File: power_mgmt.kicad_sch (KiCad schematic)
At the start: 54 parts

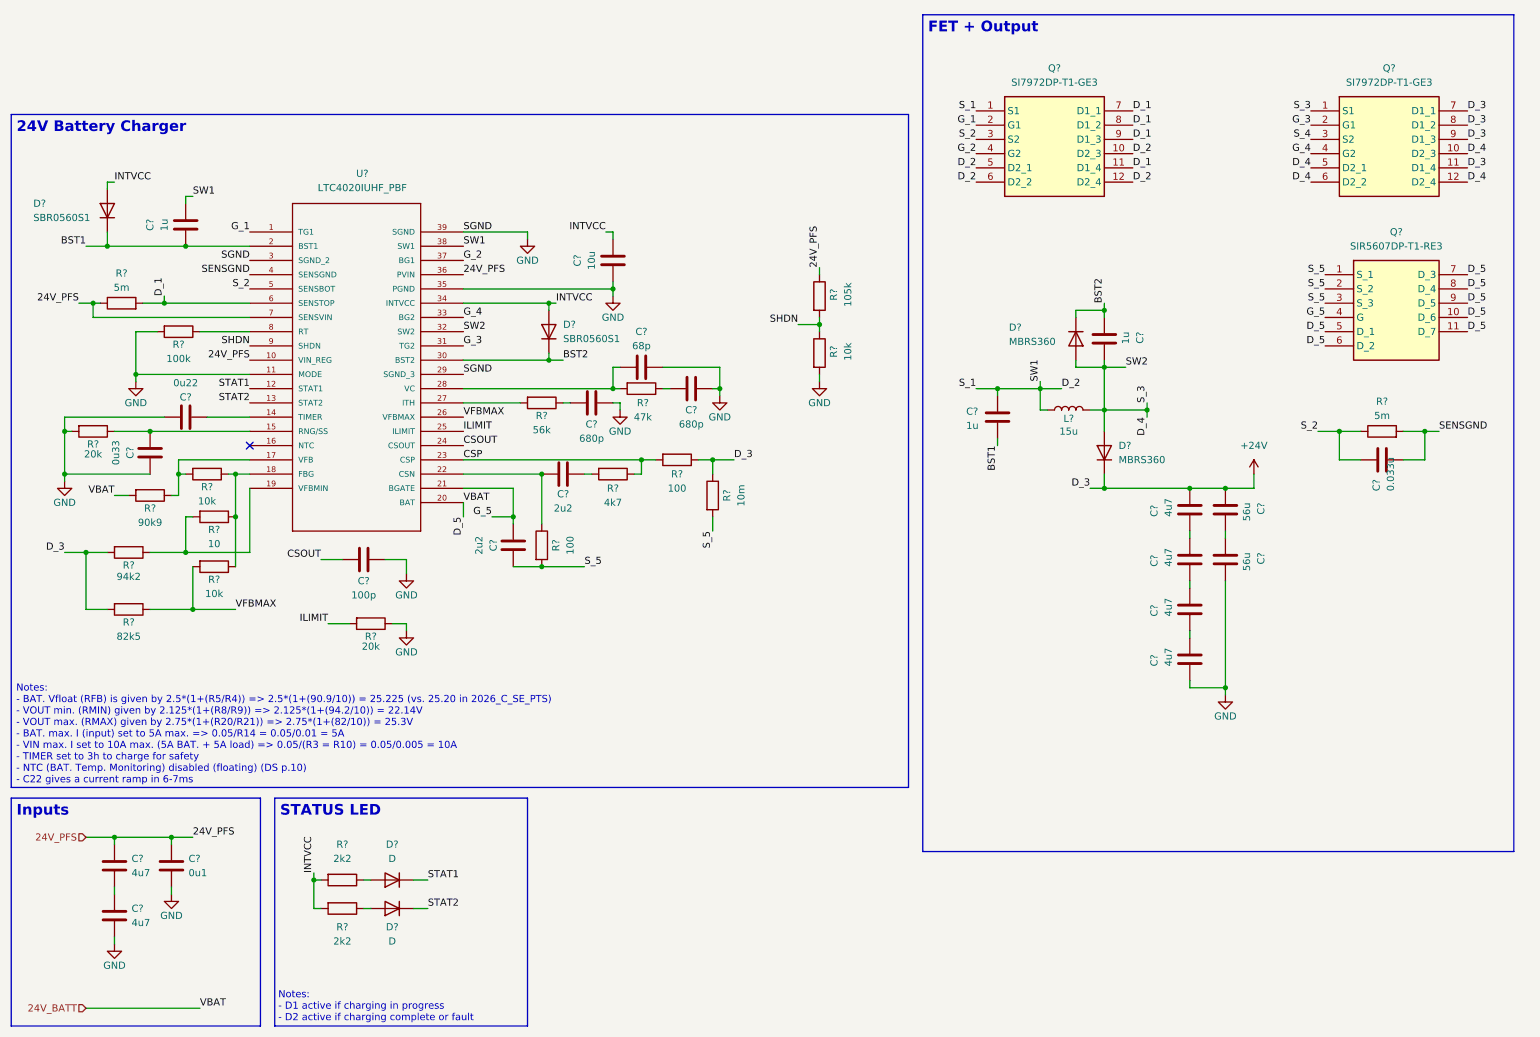
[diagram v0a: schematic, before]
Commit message: add: power MUX + global labels
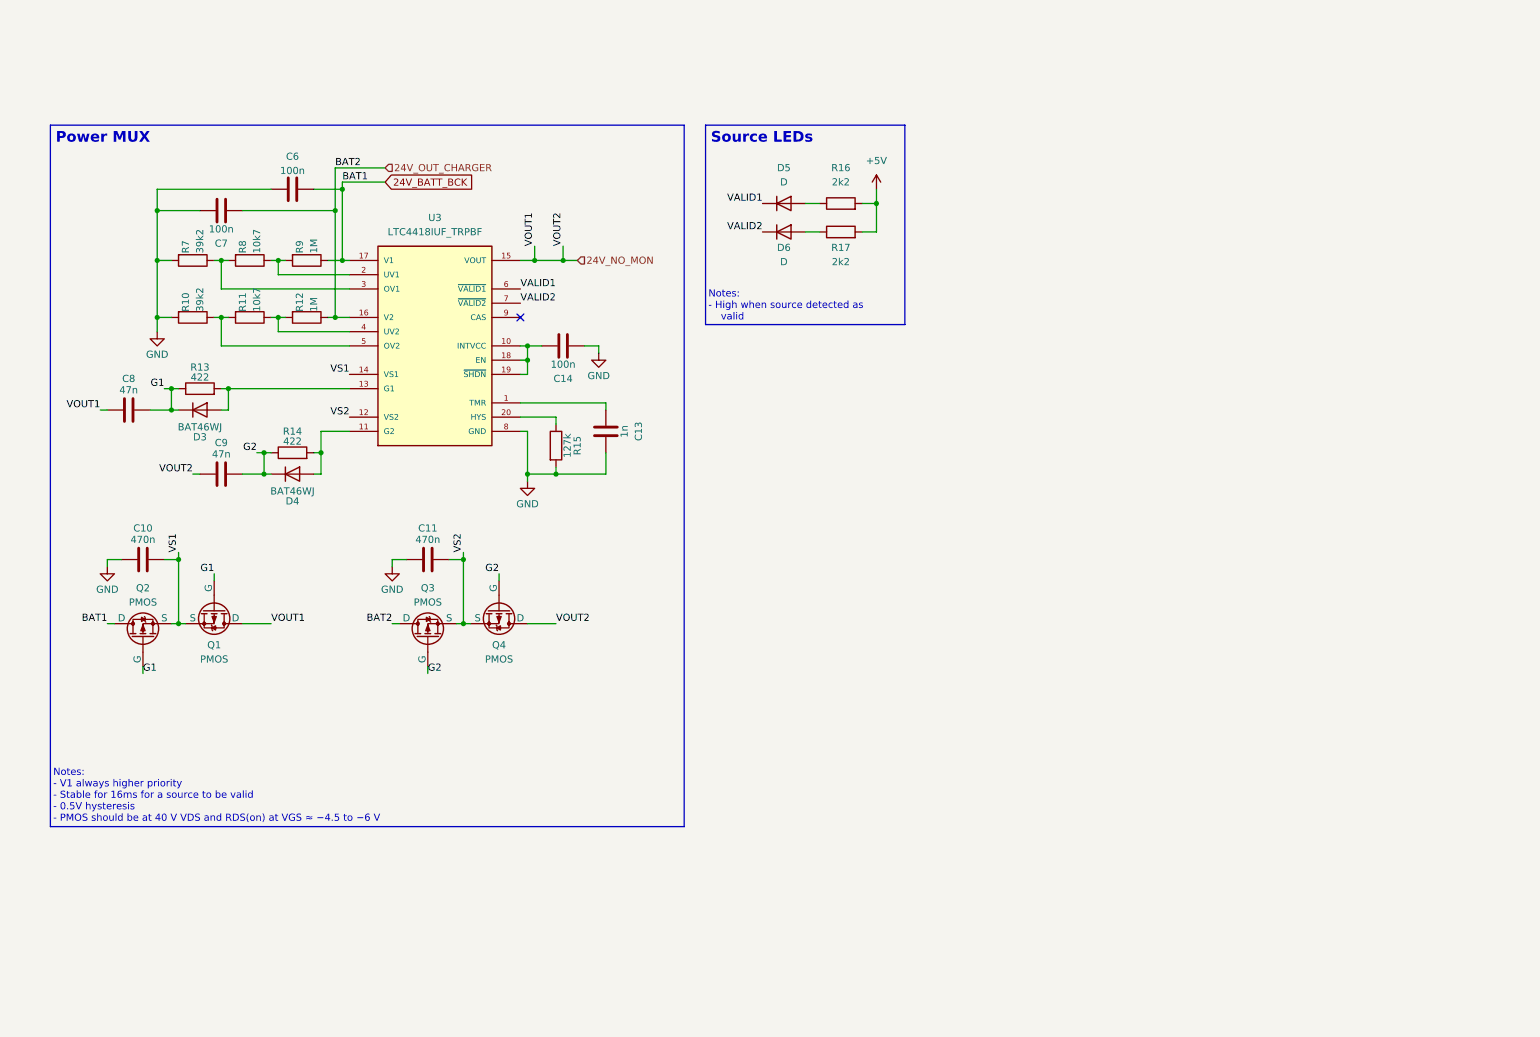
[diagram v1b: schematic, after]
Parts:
- removed C? (x6): 4u7, symbol Device:C
- removed C?: 0u22, symbol Device:C
- removed C? (x2): 680p, symbol Device:C
- removed C?: 68p, symbol Device:C
- removed C? (x3): 1u, symbol Device:C
- removed C?: 10u, symbol Device:C
- removed C? (x2): 56u, symbol Device:C
- removed C?: 0.033u, symbol Device:C
- removed C?: 0u1, symbol Device:C
- removed C? (x2): 2u2, symbol Device:C
- removed C?: 0u33, symbol Device:C
- removed C?: 100p, symbol Device:C
- removed D? (x2): D, symbol Device:D
- removed D? (x2): MBRS360, symbol Device:D
- removed D? (x2): SBR0560S1, symbol Device:D
- removed L?: 15u, symbol Device:L
- removed Q?: SIR5607DP-T1-RE3, SI7852ADPT1GE3, symbol SIR5607DP-T1-RE3:SIR5607DP-T1-RE3
- removed Q? (x2): SI7972DP-T1-GE3, SI7288DPT1GE3, symbol SI7972DP-T1-GE3:SI7972DP-T1-GE3
- removed R? (x2): 100, symbol Device:R
- removed R?: 10m, symbol Device:R
- removed R?: 82k5, symbol Device:R
- removed R? (x2): 5m, symbol Device:R
- removed R?: 100k, symbol Device:R
- removed R?: 94k2, symbol Device:R
- removed R? (x2): 2k2, symbol Device:R
- removed R?: 10, symbol Device:R
- removed R?: 47k, symbol Device:R
- removed R?: 90k9, symbol Device:R
- removed R? (x2): 20k, symbol Device:R
- removed R?: 105k, symbol Device:R
- removed R? (x3): 10k, symbol Device:R
- removed R?: 56k, symbol Device:R
- removed R?: 4k7, symbol Device:R
- removed U?: LTC4020IUHF_PBF, LTC4020IUHF_PBF:QFN-38_UHF, symbol LTC4020IUHF_PBF:LTC4020IUHF_PBF
- added C10, C11: 470n, symbol Device:C
- added C13: 1n, symbol Device:C
- added C14, C6, C7: 100n, symbol Device:C
- added C8, C9: 47n, symbol Device:C
- added D3, D4: BAT46WJ, symbol Device:D
- added D5, D6: D, symbol Device:D
- added Q1, Q2, Q3, Q4: PMOS, symbol Simulation_SPICE:PMOS
- added R10, R7: 39k2, symbol Device:R
- added R11, R8: 10k7, symbol Device:R
- added R12, R9: 1M, symbol Device:R
- added R13, R14: 422, symbol Device:R
- added R15: 127k, symbol Device:R
- added R16, R17: 2k2, symbol Device:R
- added U3: LTC4418IUF_TRPBF, LTC4418IUF_TRPBF:QFN50P400X400X80-21N, symbol LTC4418IUF_TRPBF:LTC4418IUF_TRPBF
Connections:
- net GND: now also C10.1, C11.1, C13.2, C14.1, C6.1, C7.2, R10.2, R15.2, R7.2, U3.21 (GND), U3.8 (GND)
- new net: R10.1, R11.2, U3.5 (OV2)
- new net: D6.2 (A), R17.1
- new net: D4.2 (A), R14.2, U3.11 (G2)
- new net: D5.2 (A), R16.1
- new net: C13.1, U3.1 (TMR)
- new net: C14.2, U3.10 (INTVCC), U3.18 (EN), U3.19 (~{SHDN})
- new net: D3.2 (A), R13.2, U3.13 (G1)
- new net: R8.1, R9.2, U3.2 (UV1)
- new net: R15.1, U3.20 (HYS)
- new net: R7.1, R8.2, U3.3 (OV1)
- new net: R11.1, R12.2, U3.4 (UV2)
- new net +5V: R16.2, R17.2
- new net 24V_BATT_BCK: C6.2, Q2.1 (D), R9.1, U3.17 (V1)
- new net 24V_NO_MON: C8.1, C9.1, Q1.1 (D), Q4.1 (D), U3.15 (VOUT)
- new net 24V_OUT_CHARGER: C7.1, Q3.1 (D), R12.1, U3.16 (V2)
- new net G1: C8.2, D3.1 (K), Q1.2 (G), Q2.2 (G), R13.1
- new net G2: C9.2, D4.1 (K), Q3.2 (G), Q4.2 (G), R14.1
- new net VALID1: D5.1 (K), U3.6 (~{VALID1})
- new net VALID2: D6.1 (K), U3.7 (~{VALID2})
- new net VS1: C10.2, Q1.3 (S), Q2.3 (S), U3.14 (VS1)
- new net VS2: C11.2, Q3.3 (S), Q4.3 (S), U3.12 (VS2)
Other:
- note added: "Notes: - High when source detected as valid"
- note added: "Notes: - V1 always higher priority - Stable for 16ms for a source to be valid - 0.5V hysteresis - PMOS should be at 40 V VDS and RDS(on) at VGS ≈ −4.5 to −6 V"
- note removed: "Notes: - BAT. Vfloat (RFB) is given by 2.5*(1+(R5/R4)) => 2.5*(1+(90.9/10)) = 25.225 (vs. 25.20 in 2026_C_SE_PTS) - VOUT min. (RMIN) given by 2.125*(1+(R8/R9)) => 2.125*(1+(94.2/10)) = 22.14V - VOUT max. (RMAX) given by 2.75*(1+(R20/R21)) => 2.75*(1+(82/10)) = 25.3V - BAT. max. I (input) set to 5A max. => 0.05/R14 = 0.05/0.01 = 5A - VIN max. I set to 10A max. (5A BAT. + 5A load) => 0.05/(R3 = R10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"
- note removed: "Notes: - D1 active if charging in progress - D2 active if charging complete or fault"
- title: FH2 - Spine -> (none)

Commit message: add: regulator + monitoring
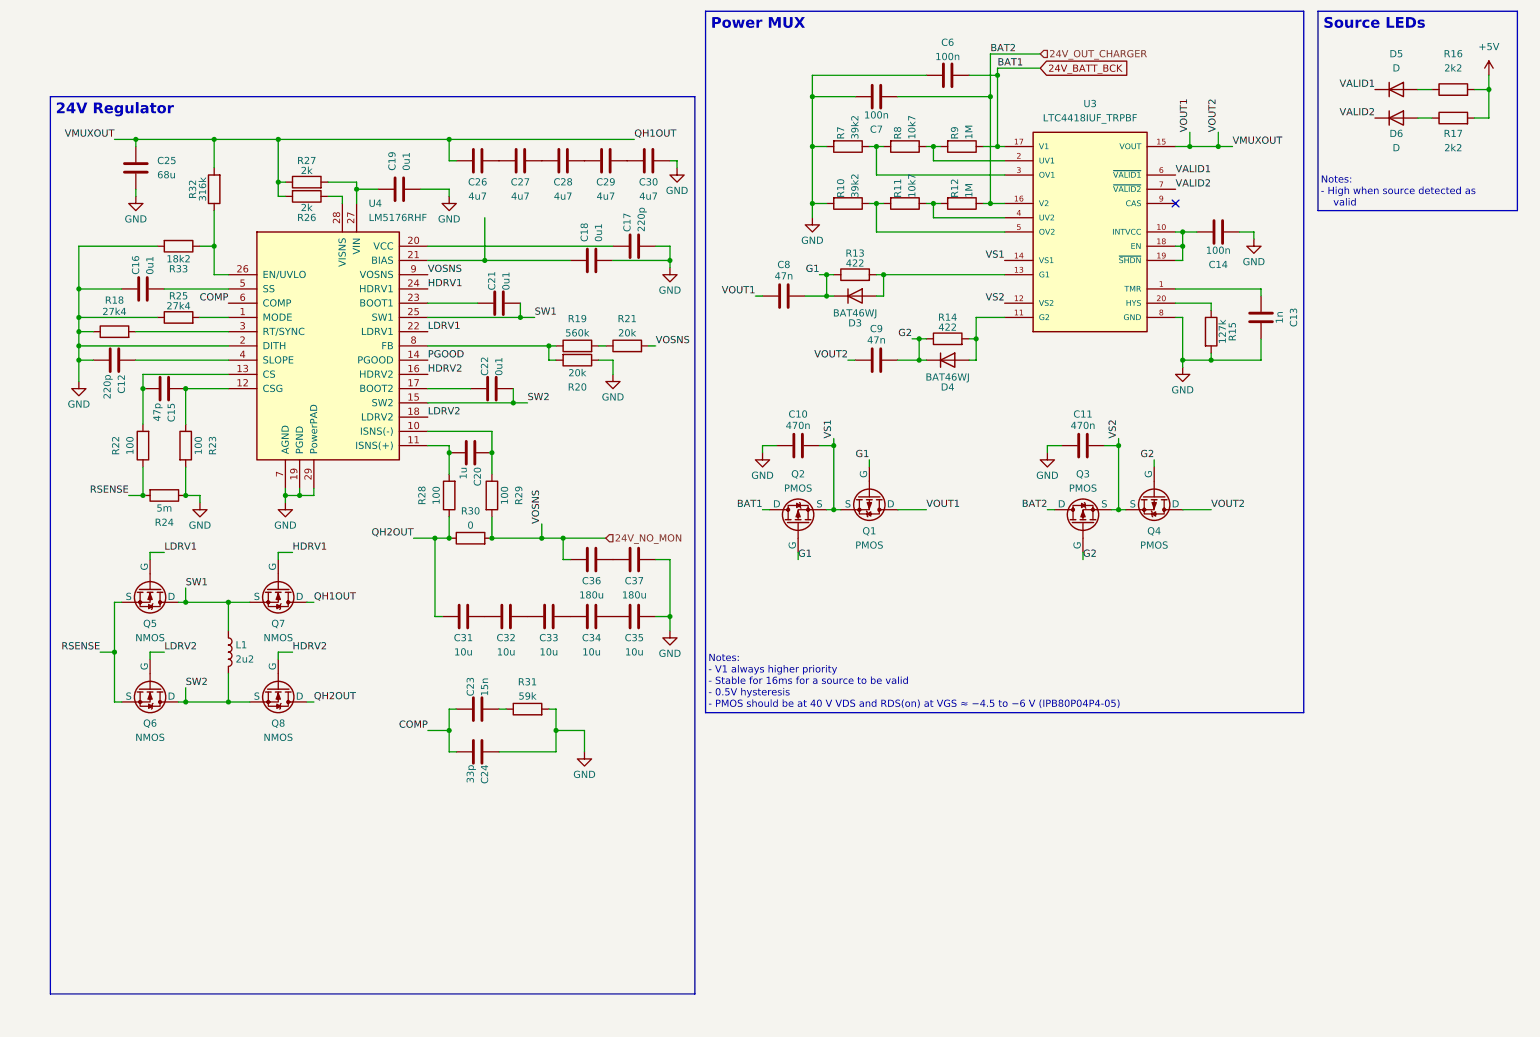
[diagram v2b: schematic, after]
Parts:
- added C12, C17: 220p, symbol Device:C
- added C15: 47p, symbol Device:C
- added C16, C18, C19, C21, C22: 0u1, symbol Device:C
- added C20: 1u, symbol Device:C
- added C23: 15n, symbol Device:C
- added C24: 33p, symbol Device:C
- added C25: 68u, symbol Device:C
- added C26, C27, C28, C29, C30: 4u7, symbol Device:C
- added C31, C32, C33, C34, C35: 10u, symbol Device:C
- added C36, C37: 180u, symbol Device:C
- added L1: 2u2, symbol Device:L
- added Q5, Q6, Q7, Q8: NMOS, symbol Simulation_SPICE:NMOS
- added R18, R25: 27k4, symbol Device:R
- added R19: 560k, symbol Device:R
- added R20, R21: 20k, symbol Device:R
- added R22, R23, R28, R29: 100, symbol Device:R
- added R24: 5m, symbol Device:R
- added R26, R27: 2k, symbol Device:R
- added R30: 0, symbol Device:R
- added R31: 59k, symbol Device:R
- added R32: 316k, symbol Device:R
- added R33: 18k2, symbol Device:R
- added U4: LM5176RHF, Package_DFN_QFN:VQFN-28-1EP_4x5mm_P0.5mm_EP2.55x3.55mm, symbol Regulator_Switching:LM5176RHF
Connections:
- net 24V_NO_MON: now also C36.2, R21.2, R29.2, R30.2, U4.9 (VOSNS); no longer C8.1, C9.1, Q1.1 (D), Q4.1 (D), U3.15 (VOUT)
- net GND: now also C12.2, C16.1, C17.2, C18.2, C19.2, C24.1, C25.2, C30.1, C35.1, C37.1, R18.1, R20.1, R23.2, R24.1, R25.1, R31.2, R33.2, U4.19 (PGND), U4.2 (DITH), U4.29 (PowerPAD), U4.7 (AGND)
- new net: R19.1, R20.2, U4.8 (FB)
- new net: R19.2, R21.1
- new net: R25.2, U4.1 (MODE)
- new net: C20.1, R29.1, U4.10 (ISNS(-))
- new net: C20.2, R28.2, U4.11 (ISNS(+))
- new net: C15.1, R23.1, U4.12 (CSG)
- new net: C15.2, R22.2, U4.13 (CS)
- new net: C22.1, U4.17 (BOOT2)
- new net: C17.1, U4.20 (VCC)
- new net: C18.1, U4.21 (BIAS)
- new net: C21.1, U4.23 (BOOT1)
- new net: R32.1, R33.1, U4.26 (EN/UVLO)
- new net: C19.1, R27.2, U4.27 (VIN)
- new net: R26.1, U4.28 (VISNS)
- new net: R18.2, U4.3 (RT/SYNC)
- new net: C12.1, U4.4 (SLOPE)
- new net: C16.2, U4.5 (SS)
- new net: C23.2, R31.1
- new net: C36.1, C37.2
- new net: C34.1, C35.2
- new net: C33.1, C34.2
- new net: C29.1, C30.2
- new net: C31.1, C32.2
- new net: C26.1, C27.2
- new net: C27.1, C28.2
- new net: C28.1, C29.2
- new net: C32.1, C33.2
- new net COMP: C23.1, C24.2, U4.6 (COMP)
- new net HDRV1: Q7.2 (G), U4.24 (HDRV1)
- new net HDRV2: Q8.2 (G), U4.16 (HDRV2)
- new net LDRV1: Q5.2 (G), U4.22 (LDRV1)
- new net LDRV2: Q6.2 (G), U4.18 (LDRV2)
- new net PGOOD: U4.14 (PGOOD)
- new net QH1OUT: C25.1, C26.2, C8.1, C9.1, Q1.1 (D), Q4.1 (D), Q7.1 (D), R26.2, R27.1, R32.2, U3.15 (VOUT)
- new net QH2OUT: C31.2, Q8.1 (D), R28.1, R30.1
- new net RSENSE: Q5.3 (S), Q6.3 (S), R22.1, R24.2
- new net SW1: C21.2, L1.1, Q5.1 (D), Q7.3 (S), U4.25 (SW1)
- new net SW2: C22.2, L1.2, Q6.1 (D), Q8.3 (S), U4.15 (SW2)
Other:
- note added: "Notes: - V1 always higher priority - Stable for 16ms for a source to be valid - 0.5V hysteresis - PMOS should be at 40 V VDS and RDS(on) at VGS ≈ −4.5 to −6 V (IPB80P04P4-05)"
- note removed: "Notes: - V1 always higher priority - Stable for 16ms for a source to be valid - 0.5V hysteresis - PMOS should be at 40 V VDS and RDS(on) at VGS ≈ −4.5 to −6 V"
- moved on the sheet: C10, C11, C13, C14, C6, C7, C8, C9, D3, D4, D5, D6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
